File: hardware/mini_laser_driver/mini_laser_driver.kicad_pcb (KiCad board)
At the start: 2 copper layers, 63 x 42 mm, 48 parts, among them J1 Conn_01x02, J2 Conn_01x02, J3 Conn_01x02, J4 Conn_01x02, J5 Conn_01x02, J6 Conn_01x02, J7 Conn_01x02, Q1 BD139, Q2 BD139, Q3 BD139, U1 LM324, U2 R-78B3.3-2.0, U3 R-78B7.2-2.0

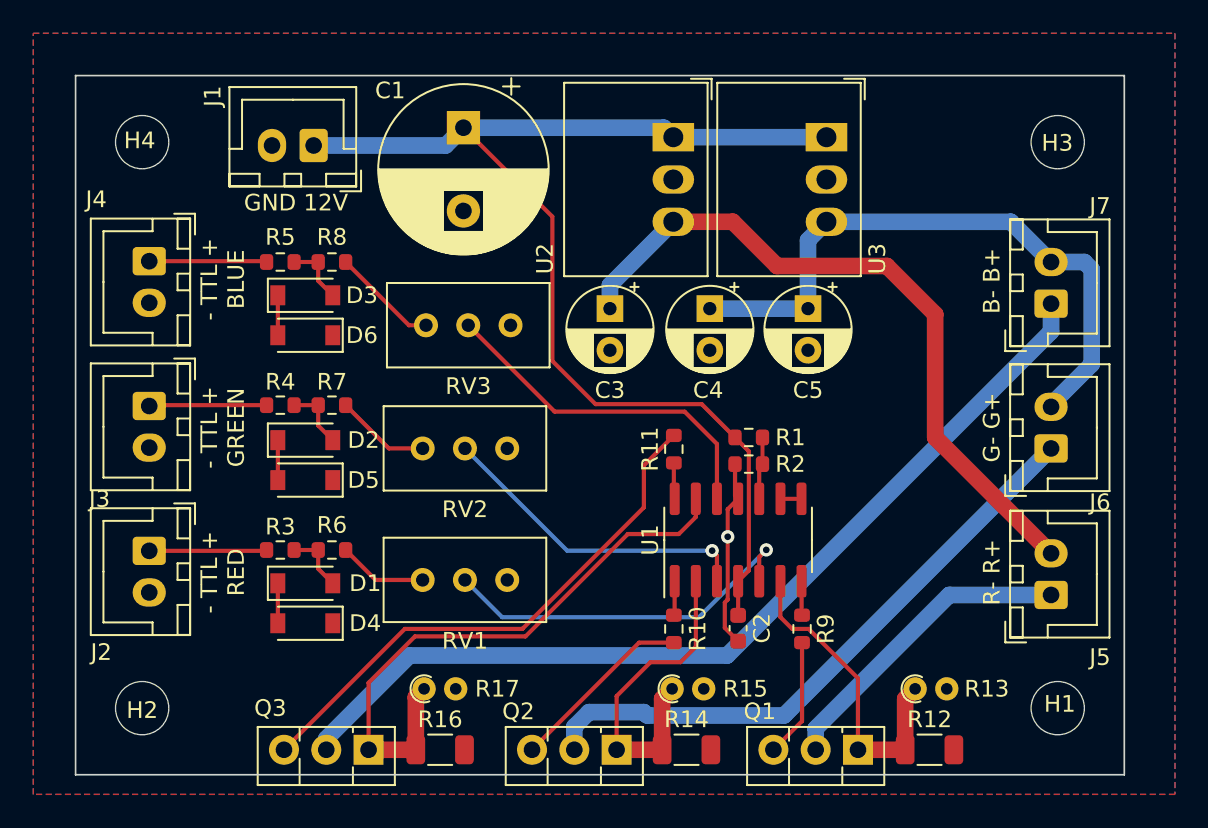
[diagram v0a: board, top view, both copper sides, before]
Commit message: Improved laser driver design
The laser driver now allows you to switch between two different brightnesses with an external switch
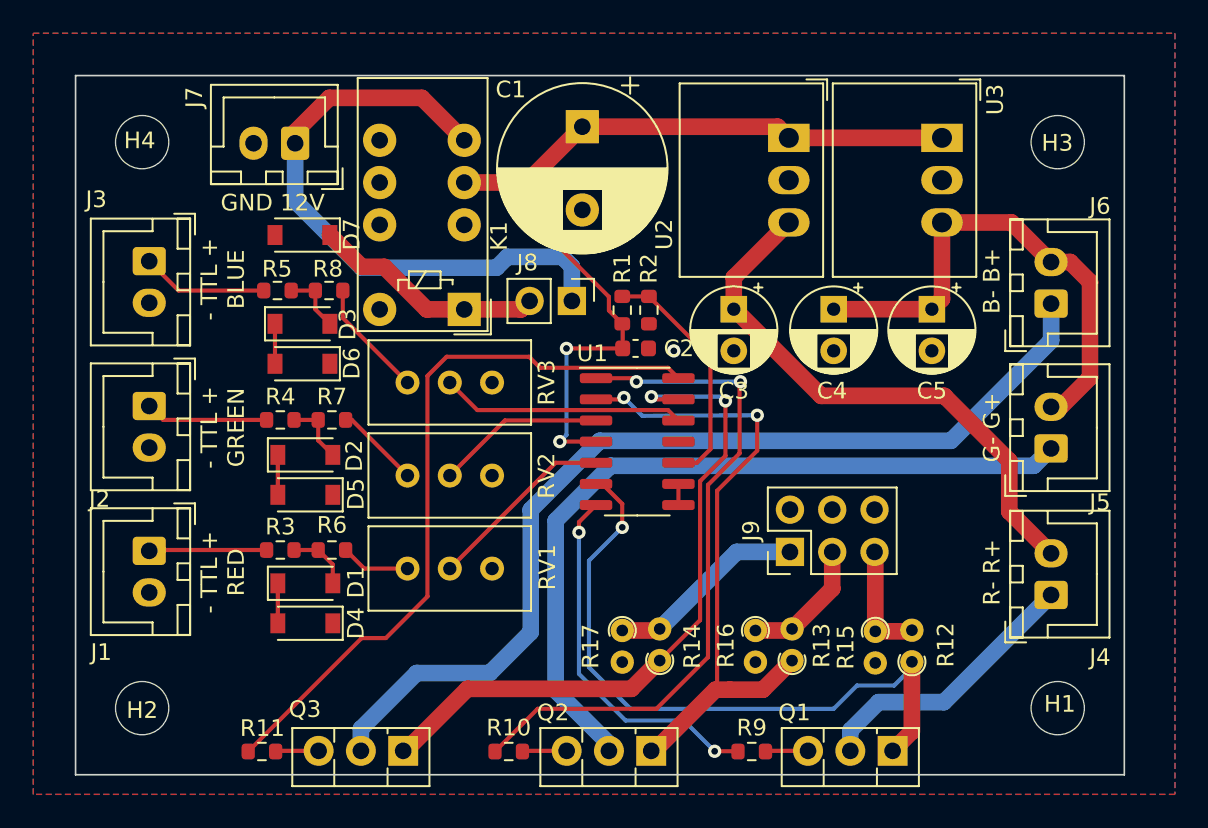
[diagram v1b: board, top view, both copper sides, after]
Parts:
- removed the R12 at (144.9, 106.4)
- removed the R14 at (130.3, 106.4)
- added D7: 1N4148W, Diode_SMD:D_SOD-123, F.Cu at (107.2, 75.4)
- added J8: Conn_01x02, Connector_PinHeader_2.54mm:PinHeader_1x02_P2.54mm_Vertical, F.Cu at (123.4, 79.4)
- added J9: Conn_02x03_Odd_Even, Connector_PinHeader_2.54mm:PinHeader_2x03_P2.54mm_Vertical, F.Cu at (136.5, 94.5)
- added K1: G6S-2, Relay_THT:Relay_DPDT_Omron_G6S-2, F.Cu at (116.9, 79.9)
- added R15: SHUNT2, Resistor_THT:R_Axial_DIN0204_L3.6mm_D1.6mm_P1.90mm_Vertical, F.Cu at (141.6, 99.2)
- added R17: SHUNT2, Resistor_THT:R_Axial_DIN0204_L3.6mm_D1.6mm_P1.90mm_Vertical, F.Cu at (126.4, 99.2)
- R12: renamed from R13; value DNP -> SHUNT1
- R13: renamed from R15; value DNP -> SHUNT1
- R14: renamed from R17; value DNP -> SHUNT1
- R16: value 10 -> SHUNT2; footprint Resistor_SMD:R_1206_3216Metric -> Resistor_THT:R_Axial_DIN0204_L3.6mm_D1.6mm_P1.90mm_Vertical
- moved R11 30.7 mm to (104.8, 106.5), turned to 0 degrees
- moved R16 20.2 mm to (134.4, 99.2), turned to -90 degrees
- moved C2 17.9 mm to (127.2, 82.2), turned to 0 degrees
- moved R14 14.3 mm to (128.7, 101.0), turned to 90 degrees
- moved R10 12.4 mm to (119.6, 106.5), turned to 0 degrees
- moved R2 11.0 mm to (128.0, 80.0), turned to 90 degrees
- moved R1 10.8 mm to (126.4, 80.0), turned to -90 degrees
- moved U1 8.46 mm to (127.3, 87.8), turned to 0 degrees
- moved R9 7.96 mm to (134.2, 106.5), turned to 0 degrees
- moved C3 7.44 mm to (133.1, 79.9)
- moved C4 7.44 mm to (139.1, 79.9)
- moved C5 7.44 mm to (145.0, 79.9)
- moved R13 7.40 mm to (136.6, 101.0), turned to 90 degrees
- moved C1 7.14 mm to (124.0, 68.9)
- moved U2 6.94 mm to (136.4, 69.6)
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- renumbered J2 to J1, J3 to J2, J4 to J3, J5 to J4, J6 to J5, J7 to J6, J1 to J7
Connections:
- J7 pad 1: +12V -> Net-(J7-Pad1)
- R12 pad 2: GND -> Net-(R12-Pad2)
- R13 pad 2: GND -> Net-(J9-Pad3)
- R14 pad 2: GND -> Net-(J9-Pad1)
- R16 pad 1: Net-(Q3-Pad1) -> Net-(J9-Pad3)
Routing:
- net Net-(R11-Pad1): track 2.18 -> 44.0 mm
- net Net-(R10-Pad1): track 2.06 -> 41.3 mm, vias 0 -> 2
- net Net-(J7-Pad1): track 0.00 -> 37.1 mm
- net Net-(Q3-Pad3): track 32.7 -> 2.60 mm
- net Net-(Q1-Pad1): track 19.4 -> 40.4 mm, vias 0 -> 1
- net Net-(R9-Pad1): track 2.05 -> 22.1 mm, vias 0 -> 2
- net Net-(Q2-Pad1): track 19.8 -> 39.0 mm, vias 0 -> 2
- net +12V: track 71.9 -> 54.0 mm, vias 0 -> 2
- net Net-(D7-Pad1): track 0.00 -> 14.1 mm
- net Net-(J9-Pad1): track 0.00 -> 12.0 mm
- net GND: track 11.4 -> 0.00 mm
- net Net-(RV1-Pad2): track 22.8 -> 11.4 mm, vias 1 -> 0
- net Net-(R1-Pad1): track 3.77 -> 14.6 mm
- net Net-(J5-Pad1): track 37.1 -> 46.7 mm
- net Net-(RV2-Pad2): track 19.3 -> 10.2 mm, vias 1 -> 0
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
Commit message: Updated laser driver silkscreen
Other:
- board text added: "3.3V"
- board text added: "7.5V"
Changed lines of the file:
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@@
+    (effects (font (size 1 1) (thickness 0.15)))
+  )
+  (gr_text "7.5V" (at 140.8 72.1 90) (layer "F.SilkS")
     (effects (font (size 1 1) (thickness 0.15)))
   )
@@
     (effects (font (size 1 1) (thickness 0.15)))
   )
+  (gr_text "3.3V" (at 131.6 72.1 90) (layer "F.SilkS")
+    (effects (font (size 1 1) (thickness 0.15)))
+  )
